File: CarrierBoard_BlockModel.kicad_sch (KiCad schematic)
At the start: 15 parts, among them J1 EDGES3D, J2 USB_C_Receptacle_USB2.0_16P, J3 Battery, SW1 BOOT, SW2 RESET, U1 USBLC6-2SC6

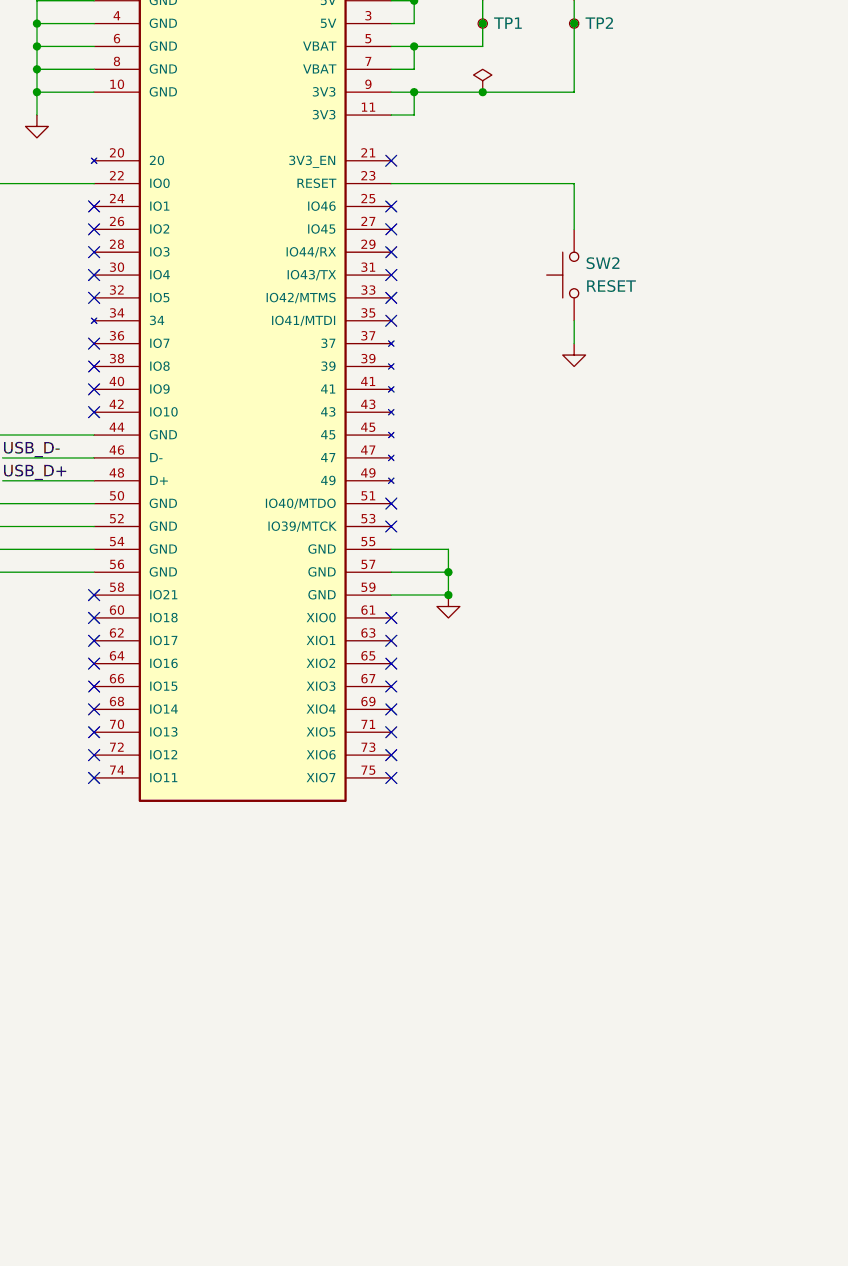
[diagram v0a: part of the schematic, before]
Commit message: Added JTAG Debugging connection Added Battery Connection
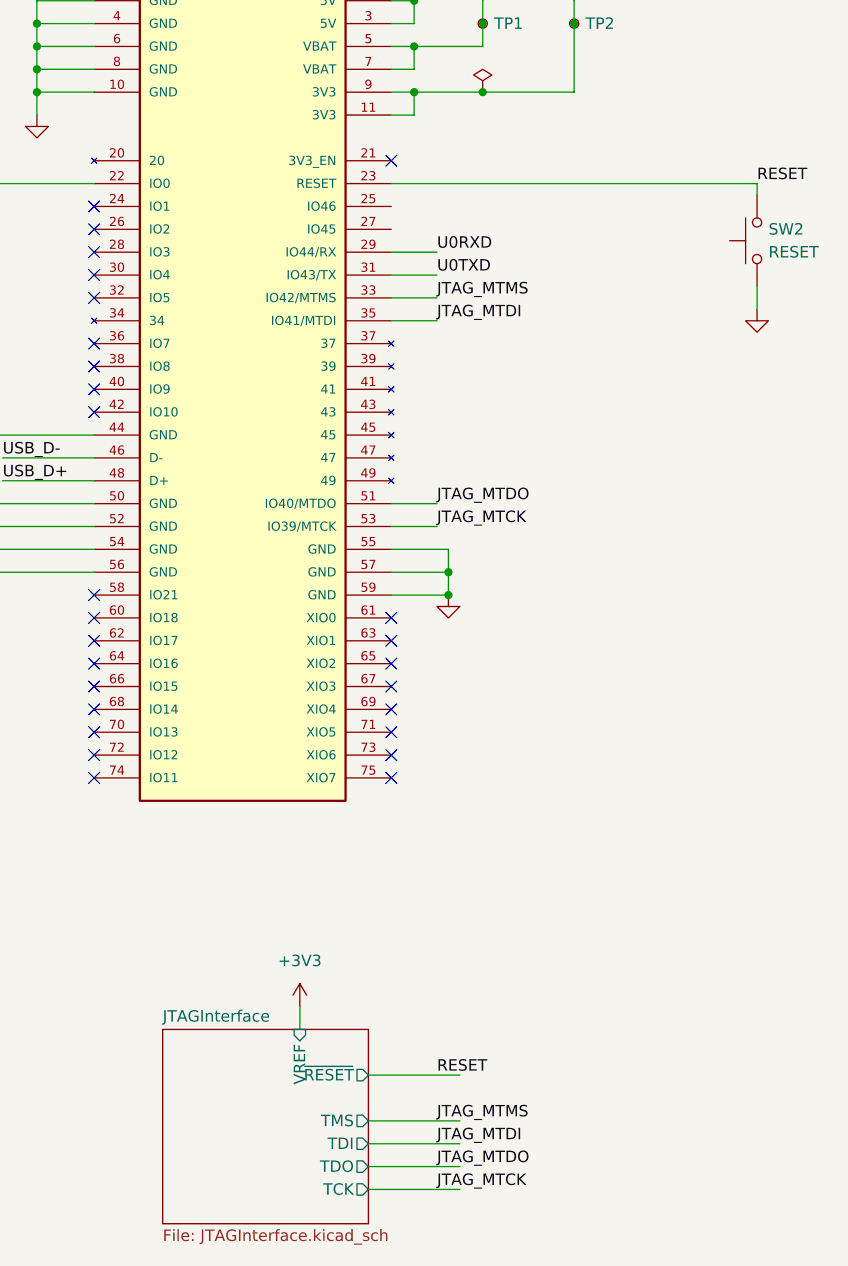
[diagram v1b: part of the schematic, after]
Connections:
- net RESET: now reaches J1.23 (RESET), SW2.2
- net U0RXD: now reaches J1.29 (IO44/RX)
- net U0TXD: now reaches J1.31 (IO43/TX)
- net JTAG_MTMS: now reaches J1.33 (IO42/MTMS)
- net JTAG_MTDI: now reaches J1.35 (IO41/MTDI)
- net JTAG_MTDO: now reaches J1.51 (IO40/MTDO)
- net JTAG_MTCK: now reaches J1.53 (IO39/MTCK)
- no-connect marks 37 -> 29
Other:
- added sheet JTAGInterface (JTAGInterface.kicad_sch)
- moved on the sheet: SW2

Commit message: Adding TMC2209 Stepper Driver
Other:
- added sheet MotorInterfaces (MotorInterfaces.kicad_sch)
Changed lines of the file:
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@@
 	(wire
 		(pts
-			(xy 162.56 157.48) (xy 172.72 157.48)
+			(xy 48.26 154.94) (xy 58.42 154.94)
 		)
 		(stroke
@@
 	(wire
 		(pts
-			(xy 162.56 154.94) (xy 172.72 154.94)
+			(xy 48.26 152.4) (xy 58.42 152.4)
 		)
 		(stroke
@@
 	(wire
 		(pts
-			(xy 154.94 137.16) (xy 154.94 139.7)
+			(xy 40.64 134.62) (xy 40.64 137.16)
 		)
 		(stroke
@@
 	(wire
 		(pts
-			(xy 162.56 152.4) (xy 172.72 152.4)
+			(xy 48.26 149.86) (xy 58.42 149.86)
 		)
 		(stroke
@@
 	(wire
 		(pts
-			(xy 162.56 144.78) (xy 172.72 144.78)
+			(xy 48.26 142.24) (xy 58.42 142.24)
 		)
 		(stroke
@@
 	(wire
 		(pts
-			(xy 162.56 149.86) (xy 172.72 149.86)
+			(xy 48.26 147.32) (xy 58.42 147.32)
 		)
 		(stroke
@@
 	)
 	(label "RESET"
-		(at 170.18 144.78 0)
+		(at 55.88 142.24 0)
 		(effects
 			(font
@@
 	)
 	(label "JTAG_MTDO"
-		(at 170.18 154.94 0)
+		(at 55.88 152.4 0)
 		(effects
 			(font
@@
 	)
 	(label "JTAG_MTMS"
-		(at 170.18 149.86 0)
+		(at 55.88 147.32 0)
 		(effects
 			(font
@@
 	)
 	(label "JTAG_MTCK"
-		(at 170.18 157.48 0)
+		(at 55.88 154.94 0)
 		(effects
 			(font
@@
 	)
 	(label "JTAG_MTDI"
-		(at 170.18 152.4 0)
+		(at 55.88 149.86 0)
 		(effects
 			(font
@@
 	(symbol
 		(lib_id "power:+3V3")
-		(at 154.94 137.16 0)
+		(at 40.64 134.62 0)
 		(unit 1)
 		(exclude_from_sim no)
@@
 		(fields_autoplaced yes)
 		(property "Reference" "#PWR022"
-			(at 154.94 140.97 0)
+			(at 40.64 138.43 0)
 			(effects
 				(font
@@
 		)
 		(property "Value" "+3V3"
-			(at 154.94 132.08 0)
+			(at 40.64 129.54 0)
 			(effects
 				(font
@@
 		)
 		(property "Footprint" ""
-			(at 154.94 137.16 0)
+			(at 40.64 134.62 0)
 			(effects
 				(font
@@
 		)
 		(property "Datasheet" ""
-			(at 154.94 137.16 0)
+			(at 40.64 134.62 0)
 			(effects
 				(font
@@
 		)
 		(property "Description" "Power symbol creates a global label with name \"+3V3\""
-			(at 154.94 137.16 0)
+			(at 40.64 134.62 0)
 			(effects
 				(font
@@
 	)
 	(sheet
-		(at 139.7 139.7)
+		(at 226.06 22.86)
+		(size 45.72 30.48)
+		(exclude_from_sim no)
+		(in_bom yes)
+		(on_board yes)
+		(dnp no)
+		(fields_autoplaced yes)
+		(stroke
+			(width 0.1524)
+			(type solid)
+		)
+		(fill
+			(color 255 229 191 1.0000)
+		)
+		(property "Sheetname" "MotorInterfaces"
+			(at 226.06 22.1484 0)
+			(effects
+				(font
+					(size 1.27 1.27)
+				)
+				(justify left bottom)
+			)
+		)
+		(property "Sheetfile" "MotorInterfaces.kicad_sch"
+			(at 226.06 53.9246 0)
+			(effects
+				(font
+					(size 1.27 1.27)
+				)
+				(justify left top)
+			)
+		)
+		(instances
+			(project "ESP32S3UMCarrierBoard"
+				(path "/5c092c18-735e-4fbc-ac2e-cfa79fa61a15/d6e8831a-ca8a-4ae1-b77a-5ce7c7004a0f"
+					(page "4")
+				)
+			)
+		)
+	)
+	(sheet
+		(at 25.4 137.16)
 		(size 22.86 21.59)
 		(exclude_from_sim no)
@@
 		)
 		(property "Sheetname" "JTAGInterface"
-			(at 139.7 138.9884 0)
+			(at 25.4 136.4484 0)
 			(effects
 				(font
@@
 		)
 		(property "Sheetfile" "JTAGInterface.kicad_sch"
-			(at 139.7 161.8746 0)
+			(at 25.4 159.3346 0)
 			(effects
 				(font
@@
 		)
 		(pin "TCK" output
-			(at 162.56 157.48 0)
+			(at 48.26 154.94 0)
 			(effects
 				(font
@@
 		)
 		(pin "TMS" output
-			(at 162.56 149.86 0)
+			(at 48.26 147.32 0)
 			(effects
 				(font
@@
 		)
 		(pin "VREF" input
-			(at 154.94 139.7 90)
+			(at 40.64 137.16 90)
 			(effects
 				(font
@@
 		)
 		(pin "TDO" output
-			(at 162.56 154.94 0)
+			(at 48.26 152.4 0)
 			(effects
 				(font
@@
 		)
 		(pin "~{RESET}" output
-			(at 162.56 144.78 0)
+			(at 48.26 142.24 0)
 			(effects
 				(font
@@
 		)
 		(pin "TDI" output
-			(at 162.56 152.4 0)
+			(at 48.26 149.86 0)
 			(effects
 				(font
